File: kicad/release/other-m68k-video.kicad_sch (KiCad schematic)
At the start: 27 parts, among them J5 RCA composite, U11 AD724JR, Y2 3.579545MHz

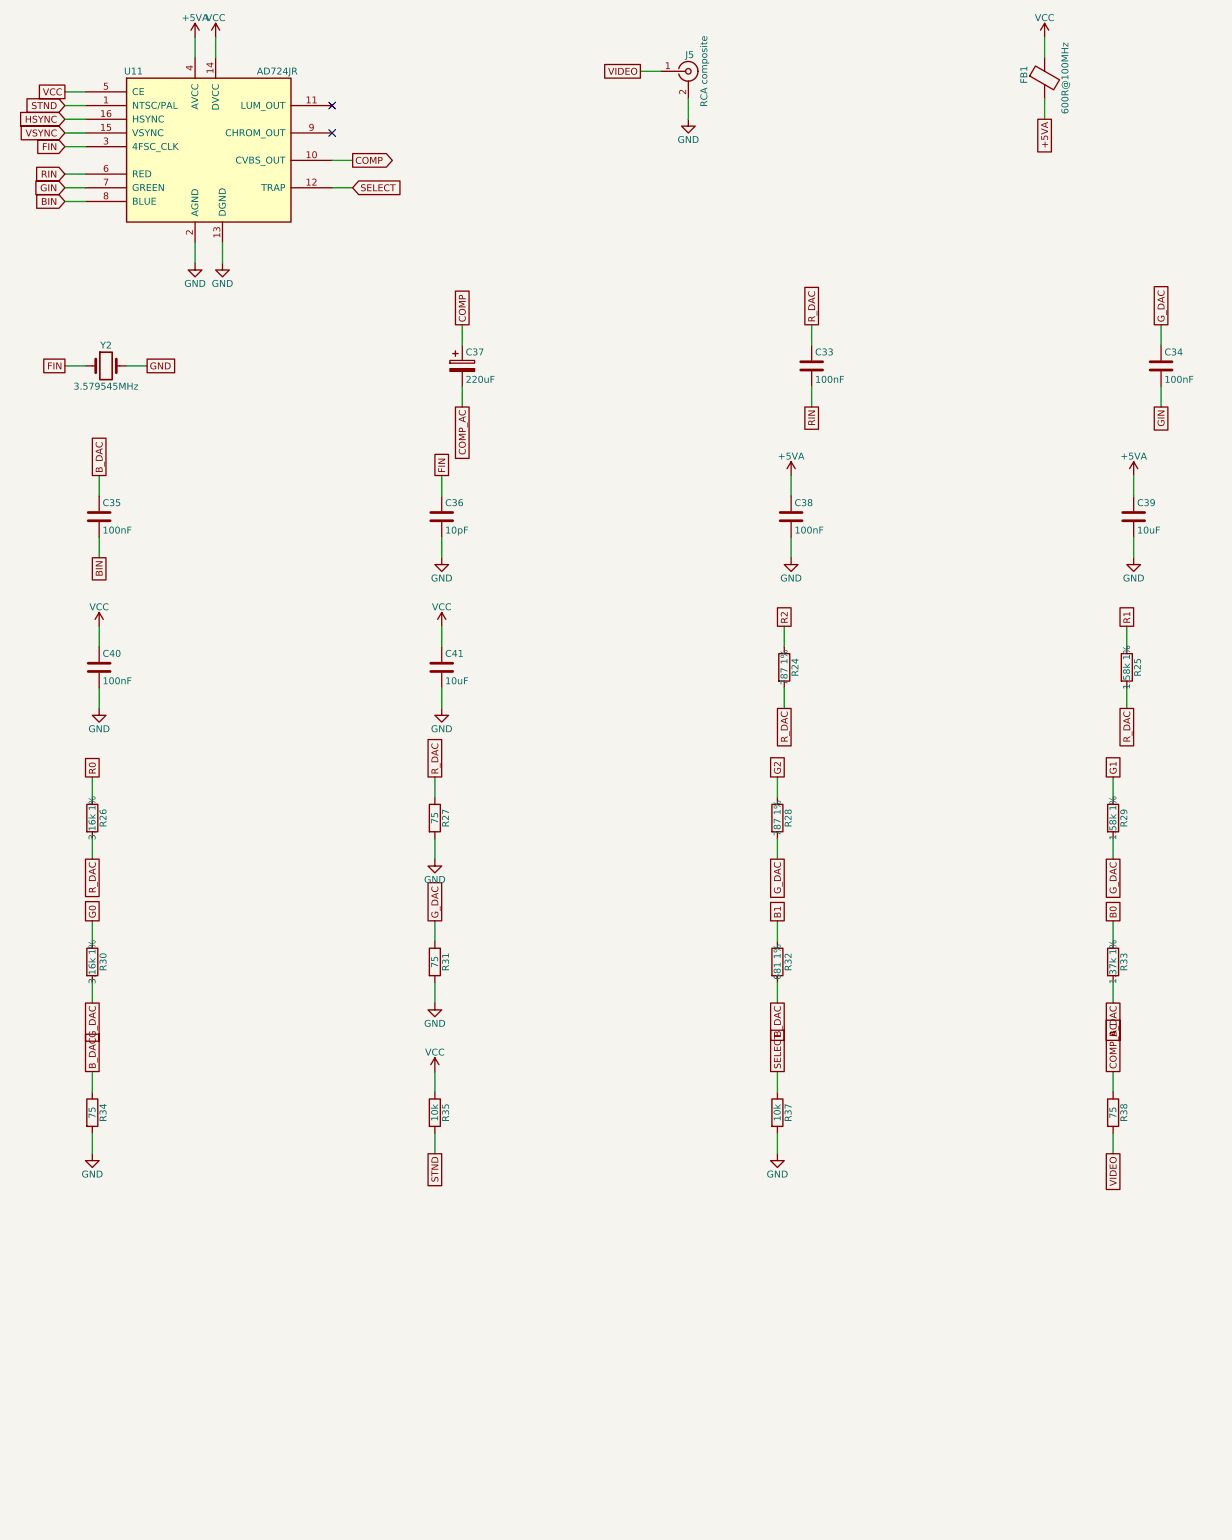
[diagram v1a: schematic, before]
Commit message: board rev C2 (spec rev 10): front and back edges, S-video jack, serial B header, dedication silkscreen
The rev B4 order was stopped; rev C2 is what goes to PCBWay. The sheet's bottom edge is the
machine's front: J3 PS/2, J6 audio, J4 microSD (LDO behind it), then SW1 RESET and SW2 NMI
with the LEDs D5 PWR, D3 LED0, D4 LED1 behind them, all labelled. The top edge is the back:
J1 USB-C, J2 serial A, J11 serial B (a second FTDI-pinout header on DUART channel B; it
replaces the 2x8 expansion header J8, which carried only channel B and the rails after spec
rev 7), J5 composite, J10 S-video (CUI MD-40SM mini-DIN 4 on the AD724's LUMA and CRMA
outputs through 220 uF and 75 ohm each; new footprint and symbol in kicad/lib). J9 (logic
analyzer) and J7 (JTAG) stand on the left edge with the six series arrays hand-placed in a
spaced column (the auto-placed cluster left one connection unroutable). The flash chips
stand vertically at the right edge; the AD724 section sits right of the S-video jack; the
bus buffers moved under the SRAMs. The open area under the CPU carries "Griffin Jr.",
"October 2026", "I love you, Kris!" and the revision; connector labels are placed where
the silkscreen checker finds them free of pads and other silk.

Routed by freerouting (optimizer on): 0 DRC violations, 0 unrouted. Fab package and
release regenerated; ORDER.md rewritten for rev C2. Spec rev 10 carries only the connector
wording (serial headers, S-video); no register or firmware change.

Co-Authored-By: Claude Fable 5.1 <noreply@anthropic.com>
Claude-Session: https://claude.ai/code/session_019bbFLKMxhKXGW6aABP44Z1
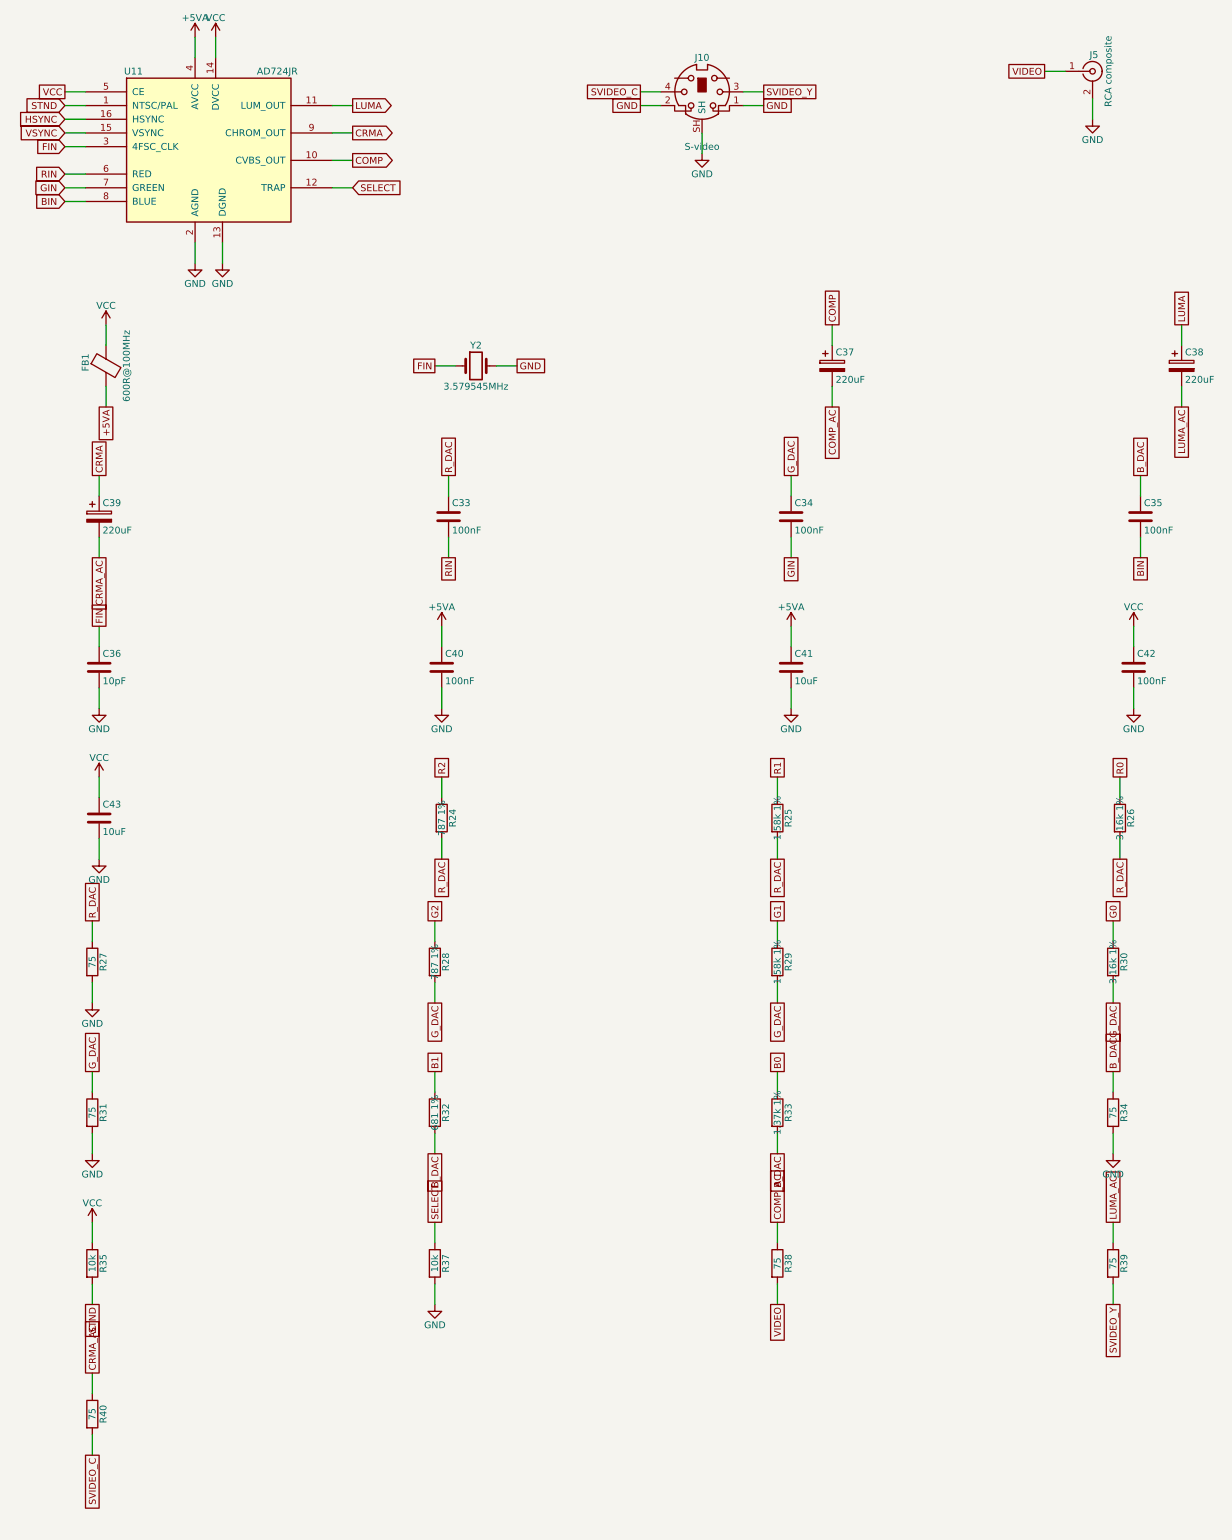
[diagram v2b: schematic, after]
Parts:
- added C42: 100nF, Capacitor_SMD:C_0603_1608Metric, symbol Device:C
- added C43: 10uF, Capacitor_SMD:C_0805_2012Metric, symbol Device:C
- added J10: S-video, other-m68k:MiniDIN-4_CUI_MD-40SM_Horizontal, symbol other-m68k:Mini-DIN-4_Shield
- added R39, R40: 75, Resistor_SMD:R_0603_1608Metric, symbol Device:R
- C38: value 100nF -> 220uF; footprint Capacitor_SMD:C_0603_1608Metric -> Capacitor_THT:CP_Radial_D6.3mm_P2.50mm; symbol Device:C -> Device:C_Polarized; Desc 100 nF 50 V X7R 0603 -> 220 uF 16 V electrolytic, 6.3 mm dia, 2.5 mm pitch; LCSC C1591 -> (none); MPN CL10B104KB8NNNC -> 16ZLH220MEFC6.3X11; Manufacturer Samsung -> Rubycon; PcbNear U11 -> J10
- C39: value 10uF -> 220uF; footprint Capacitor_SMD:C_0805_2012Metric -> Capacitor_THT:CP_Radial_D6.3mm_P2.50mm; symbol Device:C -> Device:C_Polarized; Desc 10 uF 25 V X5R 0805 -> 220 uF 16 V electrolytic, 6.3 mm dia, 2.5 mm pitch; LCSC C15850 -> (none); MPN CL21A106KAYNNNE -> 16ZLH220MEFC6.3X11; Manufacturer Samsung -> Rubycon; PcbNear U11 -> J10
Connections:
- net +5VA: now also C40.1, C41.1; no longer C38.1, C39.1
- net GND: now also C42.2, C43.2, J10.1, J10.2, J10.SH; no longer C38.2, C39.2
- net VCC: now also C42.1, C43.1; no longer C40.1, C41.1
- net LUMA: now reaches U11.11 (LUM_OUT)
- net LUMA: now also C38.1
- net CRMA: now reaches U11.9 (CHROM_OUT)
- net CRMA: now also C39.1
- new net CRMA_AC: C39.2, R40.1
- new net LUMA_AC: C38.2, R39.1
- new net SVIDEO_C: J10.4, R40.2
- new net SVIDEO_Y: J10.3, R39.2
- no-connect marks 2 -> 0
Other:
- moved on the sheet: C33, C34, C35, C36, C37, C40, C41, FB1, J5, R24, R25, R26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

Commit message: rev C3 BOM: the SRAM, flash and AD724 leave the assembly BOM (we buy and fit them); ORDER.md gets the order-form substitution note
PCBWay quoted $281 of parts for the B4 bill, $170 of it the five chips (AD724 $77,
two AS6C4008 $31, two SST39SF040 $9.76) plus $60 for two machined sockets. The chips
are now Assembly=customer / Chip_Supply=customer: the sockets ship empty, U11 is
hand-soldered here, and nothing is consigned. ORDER.md gains the socket and substitute
wording for the order form and the list of connectors to keep on the named part.

Co-Authored-By: Claude Fable 5.1 <noreply@anthropic.com>
Claude-Session: https://claude.ai/code/session_019bbFLKMxhKXGW6aABP44Z1
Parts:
- U11: Assembly pcba -> customer; Desc RGB to NTSC/PAL encoder, SOIC-16W. LAST TIME BUY (DigiKey L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 -> RGB to NTSC/PAL encoder, SOIC-16W. NOT in the assembly BOM: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
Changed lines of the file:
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@@
 			)
 		)
-		(property "Desc" "RGB to NTSC/PAL encoder, SOIC-16W. LAST TIME BUY (DigiKey LTB 2027-07-29): buy now, consign if the assembler cannot source"
+		(property "Desc" "RGB to NTSC/PAL encoder, SOIC-16W. NOT in the assembly BOM: we buy and hand-solder it (LAST TIME BUY, DigiKey LTB 2027-07-29, about $25 there against $77 quoted by PCBWay)"
 			(at 67.31 41.91 0)
 			(effects
@@
 			)
 		)
-		(property "Assembly" "pcba"
+		(property "Assembly" "customer"
 			(at 67.31 41.91 0)
 			(effects

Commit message: BOM: PCBWay descriptions carry only the part and its substitution rule; our sourcing remarks move to a Note field in parts.json, the KiCad BOM and the customer-parts list
Co-Authored-By: Claude Fable 5.1 <noreply@anthropic.com>
Claude-Session: https://claude.ai/code/session_019bbFLKMxhKXGW6aABP44Z1
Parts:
- U11: Desc RGB to NTSC/PAL encoder, SOIC-16W. NOT in the assembly BOM: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 -> RGB to NTSC/PAL encoder, SOIC-16W; Note (none) -> Not in the assembly BOM: we buy and hand-solder it. LAST TI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
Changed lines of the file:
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@@
 			)
 		)
-		(property "Desc" "RGB to NTSC/PAL encoder, SOIC-16W. NOT in the assembly BOM: we buy and hand-solder it (LAST TIME BUY, DigiKey LTB 2027-07-29, about $25 there against $77 quoted by PCBWay)"
+		(property "Desc" "RGB to NTSC/PAL encoder, SOIC-16W"
 			(at 67.31 41.91 0)
 			(effects
+				(font
+					(size 1.27 1.27)
+				)
+				(hide yes)
+			)
+		)
+		(property "Note" "Not in the assembly BOM: we buy and hand-solder it. LAST TIME BUY, DigiKey LTB 2027-07-29, about $25 there against $77 quoted by PCBWay (2026-10); buy spares for the bare boards"
+			(at 67.31 41.91 0)
+			(effects
